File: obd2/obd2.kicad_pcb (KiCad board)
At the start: 2 copper layers, 3 parts, among them U1 389-MCP2515-I/ST, U2 385-MCP2551-I/SN, U3 1389-LPC1343FBD48,151

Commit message: Moved some files around.
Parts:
- removed U1: 389-MCP2515-I/ST, Plecharts/axxkb
- removed U3: 1389-LPC1343FBD48,151, melissa/dintu

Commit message: Almost done schematic and component selections
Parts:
- added C1: 0.33uF, c_0805, F.Cu at (205.1, 140.3)
- added C10: 0.1u, c_0805, F.Cu at (227.0, 141.0)
- added C11: C, c_0805, F.Cu at (206.2, 109.7)
- added C2: 0.1uF, c_0805, F.Cu at (213.5, 145.9)
- added C3: 0.1uF, c_0805, F.Cu at (220.0, 146.0)
- added C4: 39pF, c_0805, F.Cu at (218.0, 117.0)
- added C5: 39pF, c_0805, F.Cu at (218.0, 129.0)
- added C6: 10uF, c_0805, F.Cu at (222.0, 131.0)
- added C7: 0.1u, c_0805, F.Cu at (257.0, 121.0)
- added C8: 0.1u, c_0805, F.Cu at (223.0, 123.0)
- added C9: 0.1u, c_0805, F.Cu at (226.0, 112.0)
- added D1: 3V3_ON, LED_J_LEAD, F.Cu at (227.0, 136.0)
- added J1: RJ45_BASIC, RJ45, F.Cu at (211.0, 120.0)
- added J2: MICRO_SD, SD_502702_003, F.Cu at (259.0, 117.0)
- added JP1: LCD_V_SELECT, SOLDER_JUMPER_3, F.Cu at (259.0, 105.0)
- added LCD1: LCD16X2, GDM1602K, B.Cu at (267.0, 102.0)
- added MP1: SCREW_4-40, 1pin, F.Cu at (271.0, 144.0)
- added MP2: SCREW_4-40, 1pin, F.Cu at (199.0, 144.0)
- added MP3: SCREW_4-40, 1pin, F.Cu at (199.0, 103.0)
- added MP4: SCREW_4-40, 1pin, F.Cu at (271.0, 103.0)
- added P1: JTAG_PROG, GRPB052VWQS-RC, F.Cu at (252.0, 115.0)
- added R1: 330R, R3, F.Cu at (225.0, 138.0)
- added R2: R, R3, F.Cu at (212.5, 104.2)
- added R3: 60 Ohm, R3, F.Cu at (212.5, 108.8)
- added R4: 60 Ohm, R3, F.Cu at (212.5, 106.5)
- added R5: 4k7, R3, F.Cu at (256.0, 133.0)
- added R6: 10k, R3, F.Cu at (242.0, 133.0)
- added R7: 10k, R3, F.Cu at (253.0, 133.0)
- added R8: 10k, R3, F.Cu at (266.0, 133.0)
- added SW1: SW_OFF_MOM, FSM4JSMA_pushbutton, F.Cu at (237.0, 142.0)
- added SW2: SW_OFF_MOM, FSM4JSMA_pushbutton, F.Cu at (249.0, 142.0)
- added SW3: SW_OFF_MOM, FSM4JSMA_pushbutton, F.Cu at (261.0, 142.0)
- added U1: SP7805, TO-252-3, F.Cu at (211.0, 136.0)
- added U3: LD1117, DPAK, F.Cu at (219.0, 136.0)
- added U4: 1449-LPC11C14FBD48/301,, melissa/dintu, F.Cu at (232.0, 123.0)
- added U5: MCP2561, SOIC-8-Narrow, F.Cu at (220.0, 111.0)
- added W1: VBAT_T, SIL-2, F.Cu at (199.0, 112.0)
- added W2: 5V_T, SIL-2, F.Cu at (208.0, 146.0)
- added W3: 3V3_T, SIL-2, F.Cu at (226.0, 146.0)
- added X1: 20MHz, CSM-3X, F.Cu at (217.0, 123.0)
- U2: value 385-MCP2551-I/SN -> LM335; footprint Plecharts/b6cyy -> TO92
- moved U2 99.3 mm to (260.0, 136.0), turned to 270 degrees
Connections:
- U2 pad 1: (no net) -> GND
- U2 pad 2: (no net) -> TEMP
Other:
- board outline added: 80 x 49 mm

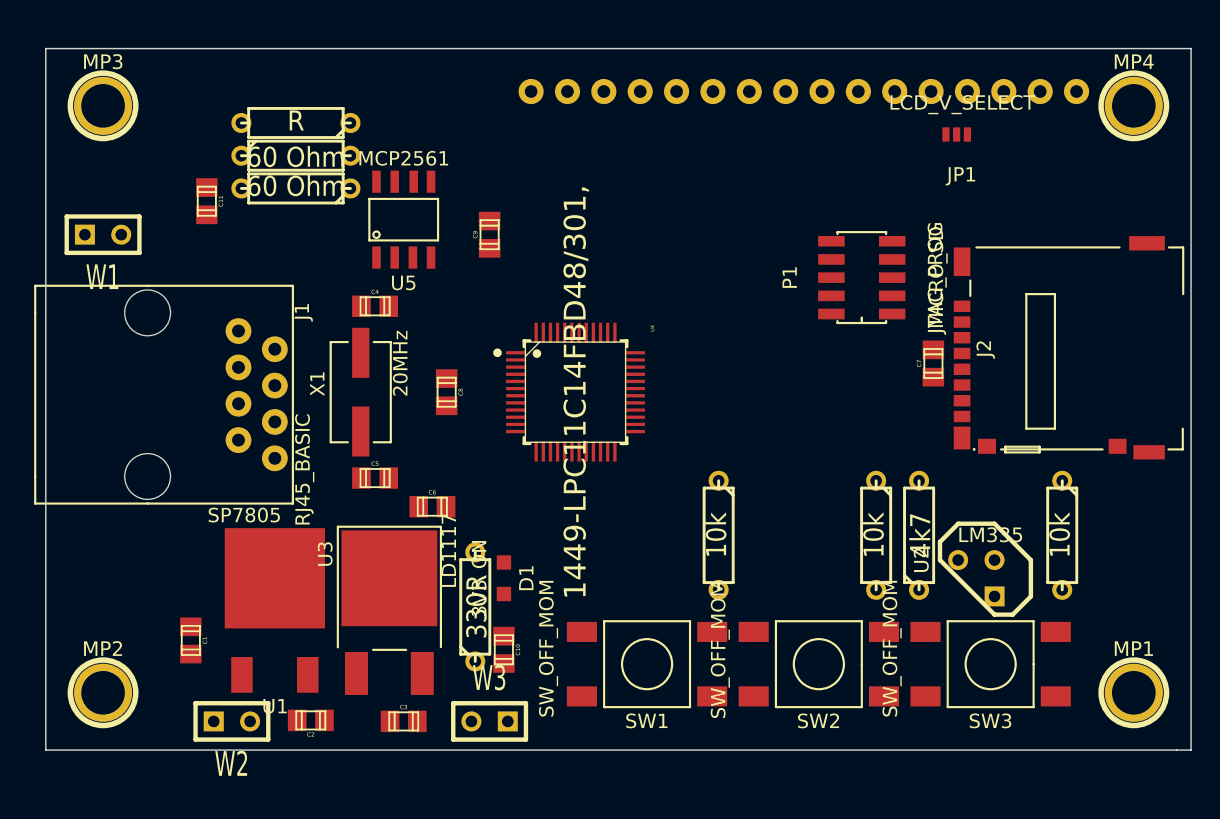
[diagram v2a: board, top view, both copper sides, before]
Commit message: All signals routed but power
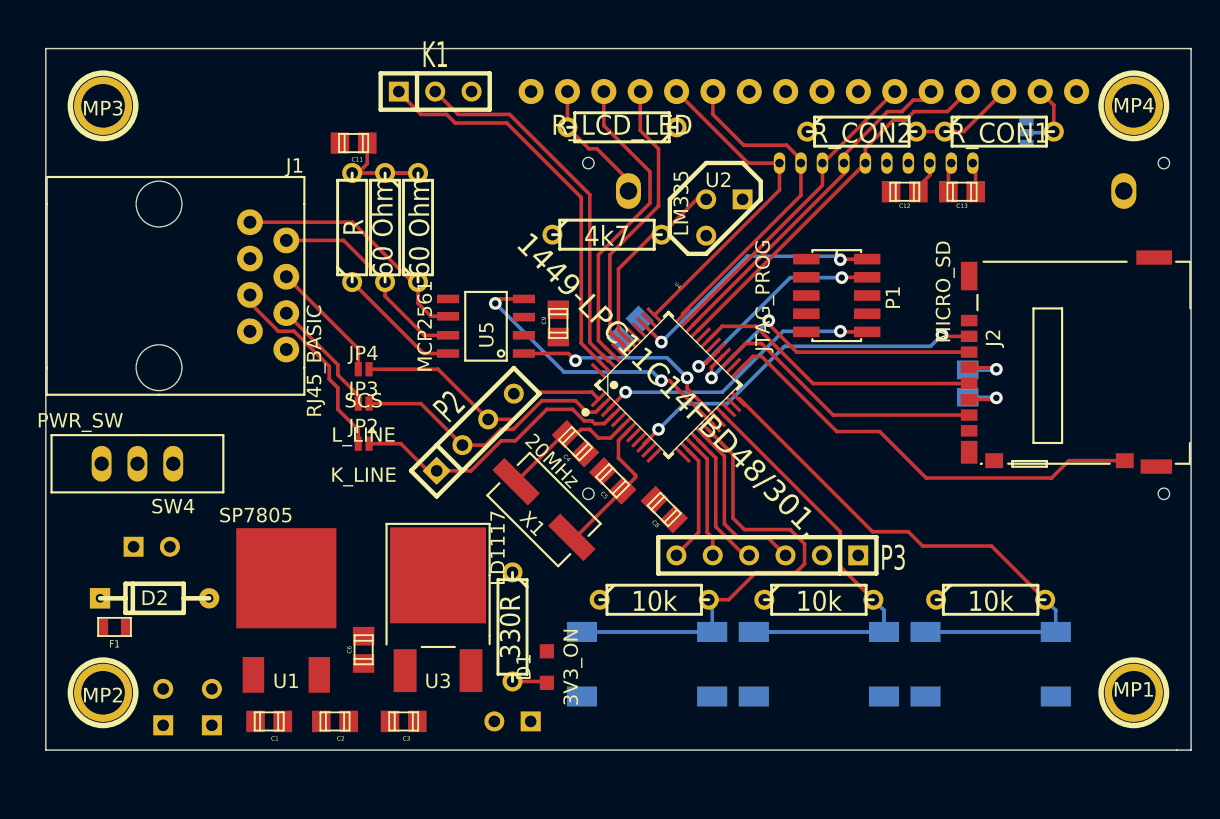
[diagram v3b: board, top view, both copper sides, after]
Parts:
- added C12: 1u, c_0805, F.Cu at (255.0, 109.0)
- added C13: 1u, c_0805, F.Cu at (259.0, 109.0)
- added D2: 1N4149, DO-35, F.Cu at (202.6, 137.4)
- added F1: approx 300mA, SM0603, F.Cu at (199.8, 139.4)
- added JP2: K_LINE, SOLDER_JUMPER, F.Cu at (217.2, 126.6)
- added JP3: L_LINE, SOLDER_JUMPER, F.Cu at (217.2, 123.8)
- added JP4: SCS, SOLDER_JUMPER, F.Cu at (217.2, 121.4)
- added K1: UART, SIL-3, F.Cu at (222.2, 102.0)
- added LCD2: LCD_COG, NHD_C0216CZ_NSW_BBW, B.Cu at (253.0, 107.0)
- added P2: IO_1, SIL-4, F.Cu at (225.0, 125.8)
- added P3: IO_2, SIL-6, F.Cu at (245.4, 134.4)
- added R10: R_CON1, R3, F.Cu at (261.6, 104.8)
- added R11: R_CON2, R3, F.Cu at (252.0, 104.8)
- added R9: R_LCD_LED, R3, F.Cu at (235.2, 104.5)
- added SW4: PWR_SW, MMS1208, F.Cu at (201.4, 128.0)
- added W4: 12V_T, SIL-2, B.Cu at (203.2, 145.0)
- C10, C7, JP1, SW1, SW2, SW3, W1, W2, W3: moved to B.Cu
- moved U2 30.7 mm to (242.4, 110.8), turned to 0 degrees
- moved R5 30.3 mm to (234.2, 112.0), turned to 0 degrees
- moved C10 24.1 mm to (235.8, 118.6), turned to 225 degrees
- moved W1 22.1 mm to (202.4, 133.8)
- moved C8 17.3 mm to (238.2, 131.2), turned to 135 degrees
- moved C4 17.0 mm to (232.0, 126.6), turned to 315 degrees
- moved C5 16.6 mm to (234.6, 129.2), turned to 135 degrees
- moved X1 15.2 mm to (229.8, 131.2), turned to 315 degrees
- moved C6 11.1 mm to (217.2, 141.0), turned to 90 degrees
- moved C11 11.0 mm to (216.5, 105.6), turned to 180 degrees
- moved U5 9.40 mm to (225.8, 118.4), turned to 90 degrees
- moved R3 8.96 mm to (221.0, 111.5), turned to 90 degrees
- moved R2 8.29 mm to (216.4, 111.5), turned to 90 degrees
- moved R4 8.00 mm to (218.7, 111.5), turned to 270 degrees
- moved C1 7.87 mm to (210.6, 146.0), turned to 180 degrees
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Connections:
- net LCD_DB4 renamed LCD_DB4/SCL
- net LCD_DB5 renamed LCD_DB5/RST
- net LCD_E renamed LCD_E/CSB
- net LCD_RS renamed LCD_RS/SI
- net LCD_RW renamed LCD_RW/RS
- C1 pad 1: VBAT -> +12V
- J1 pad 1: GND -> CAN_H
- J1 pad 2: VBAT -> CAN_L
- J1 pad 3: (no net) -> GND
- J1 pad 4: (no net) -> SCS
- J1 pad 5: (no net) -> K_LINE
- J1 pad 6: (no net) -> L_LINE
- J1 pad 7: CAN_L -> VBAT
- J1 pad 8: CAN_H -> GND
- LCD1 pad 15: (no net) -> N-0000048
- LCD1 pad 16: (no net) -> GND
- LCD1 pad 3: (no net) -> N-0000026
- U1 pad 1: VBAT -> +12V
- U4 pad 1: (no net) -> N-0000016
- U4 pad 14: (no net) -> N-0000035
- U4 pad 15: (no net) -> N-0000037
- U4 pad 16: (no net) -> N-0000038
- U4 pad 17: (no net) -> N-0000039
- U4 pad 2: (no net) -> N-0000015
- U4 pad 30: TEMP -> (no net)
- U4 pad 4: (no net) -> N-0000014
- U4 pad 42: (no net) -> TEMP
- U4 pad 45: (no net) -> LCD_DB7
- U4 pad 46: (no net) -> UART_RXD
- U4 pad 47: (no net) -> UART_TXD
- U4 pad 48: LCD_DB7 -> (no net)
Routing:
- net Button3: track 0.00 -> 38.9 mm
- net Button1: track 0.00 -> 33.2 mm
- net CARD_DETECT: track 0.00 -> 31.4 mm
- net Button2: track 0.00 -> 29.0 mm
- net UART_TXD: track 0.00 -> 28.3 mm
- net LCD_RS/SI: track 0.00 -> 26.4 mm
- net UART_RXD: track 0.00 -> 26.0 mm
- net SPI_SSEL: track 0.00 -> 26.0 mm, vias 0 -> 2
- net LCD_RW/RS: track 0.00 -> 24.2 mm
- net LCD_DB5/RST: track 0.00 -> 23.5 mm
- net LCD_DB4/SCL: track 0.00 -> 23.4 mm
- net SPI_MOSI: track 0.00 -> 22.6 mm, vias 0 -> 2
- net LCD_E/CSB: track 0.00 -> 22.0 mm
- net LCD_DB7: track 0.00 -> 21.7 mm
- net CAN_RXD: track 0.00 -> 20.9 mm, vias 0 -> 2
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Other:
- net class Default: clearance 0.254 -> 0.2032
- rule trace_clearance: 0.254 -> 0.2032
- rule trace_min: 0.254 -> 0.1524
- rule via_min_drill: 0.508 -> 0.3302
- rule via_min_size: 0.889 -> 0.508

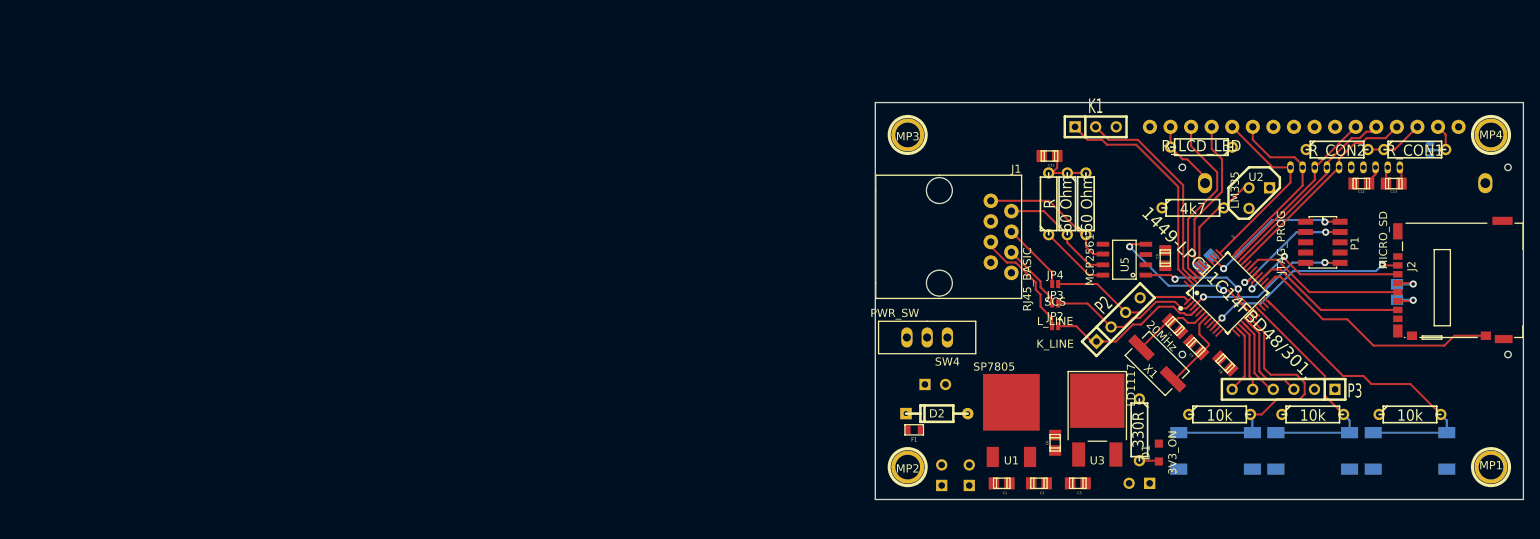
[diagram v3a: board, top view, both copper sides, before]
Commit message: Routed power and added port for UART. Added logos.
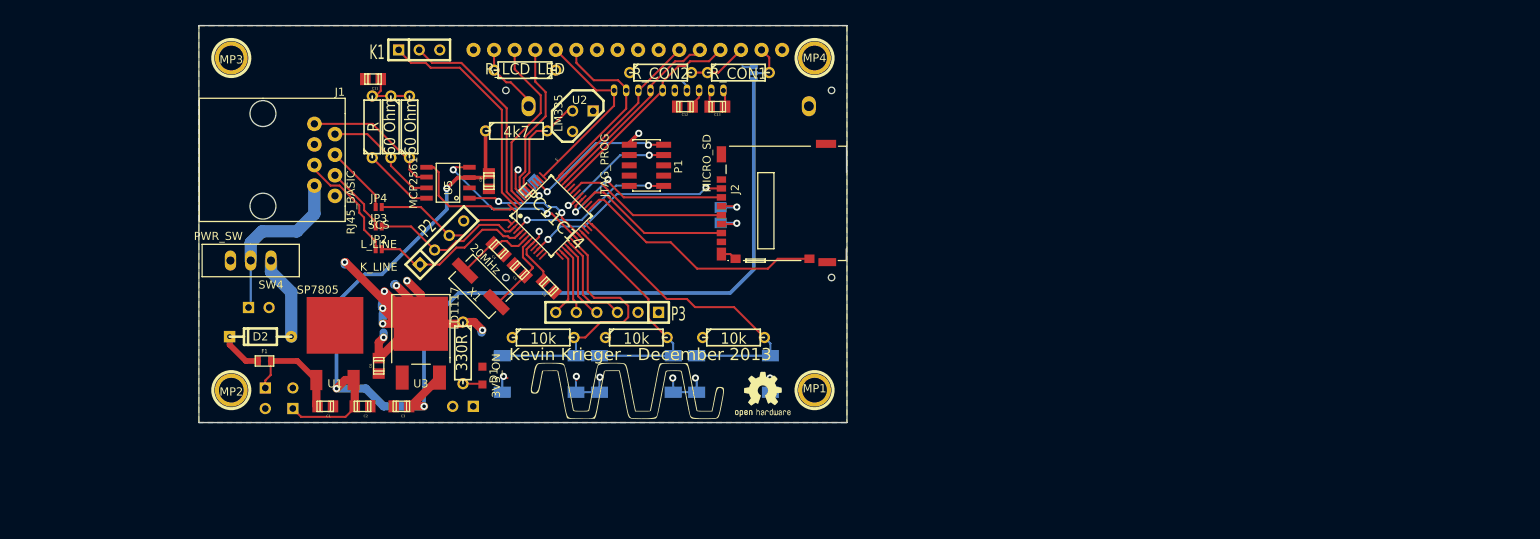
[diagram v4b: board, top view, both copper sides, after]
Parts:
- added G***: LOGO, OSHWLOGO0.3IN, F.Cu at (177.3, 131.3)
- added G***: LOGO, LOGO, F.Cu at (164.4, 134.6)
- U4: value 1449-LPC11C14FBD48/301, -> LPC11C14; footprint melissa/dintu -> LQFP48
- moved R10 84.0 mm to (178.1, 95.3)
- moved C1 84.0 mm to (127.1, 136.5)
- moved C11 84.0 mm to (133.0, 96.1)
- moved C12 84.0 mm to (171.5, 99.5)
- moved C13 84.0 mm to (175.5, 99.5)
- moved C2 84.0 mm to (131.7, 136.5)
- moved C3 84.0 mm to (136.5, 136.5)
- moved C4 84.0 mm to (148.5, 117.1)
- moved C5 84.0 mm to (151.1, 119.7)
- moved C6 84.0 mm to (133.7, 131.5)
- moved C8 84.0 mm to (154.7, 121.7)
- moved C9 84.0 mm to (147.3, 108.7)
- moved D1 84.0 mm to (146.5, 132.7)
- moved D2 84.0 mm to (119.1, 127.9)
- moved J1 84.0 mm to (128.3, 102.9)
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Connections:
- U3 pad 2: (no net) -> +3.3V
- U4 pad 48: (no net) -> CAN_XCVR_RS
- U5 pad 8: (no net) -> CAN_XCVR_RS
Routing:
- net +5V: track 0.00 -> 153.1 mm, vias 0 -> 3
- net +3.3V: track 3.96 -> 83.4 mm, vias 1 -> 12
- net GND: track 3.96 -> 28.0 mm, vias 1 -> 8
- net VBAT: track 0.00 -> 20.9 mm
- net CAN_XCVR_RS: track 0.00 -> 14.5 mm
- net +12V: track 0.00 -> 13.5 mm
- net N-0000026: track 0.00 -> 10.4 mm
- net N-0000073: track 0.00 -> 5.37 mm
- added copper zone on B.Cu, net +3.3V
- added copper zone on F.Cu, net GND
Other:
- board text added: "Kevin Krieger - December 2013"
